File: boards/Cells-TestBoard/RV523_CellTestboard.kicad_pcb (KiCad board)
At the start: 4 copper layers, 100 x 100 mm, 26 parts

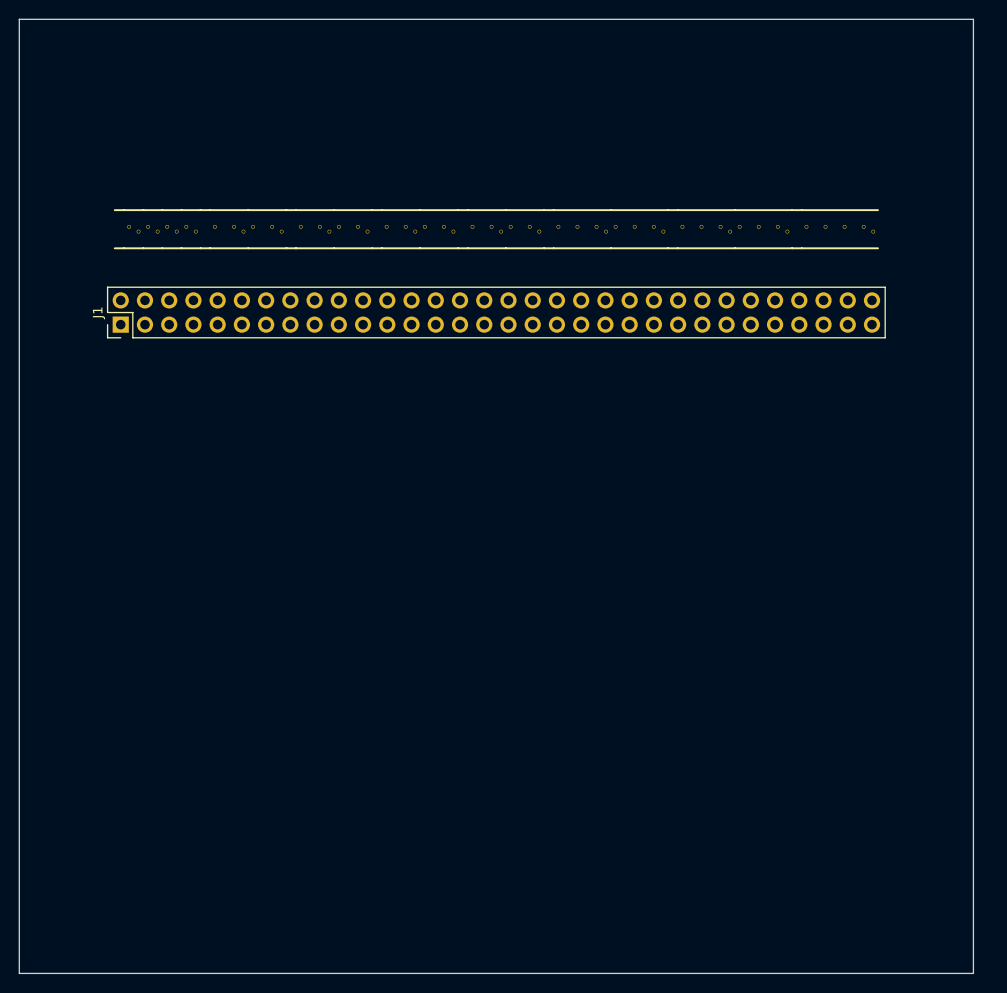
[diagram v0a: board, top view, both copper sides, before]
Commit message: Cell test board: all components placed and routed, except supply rails.
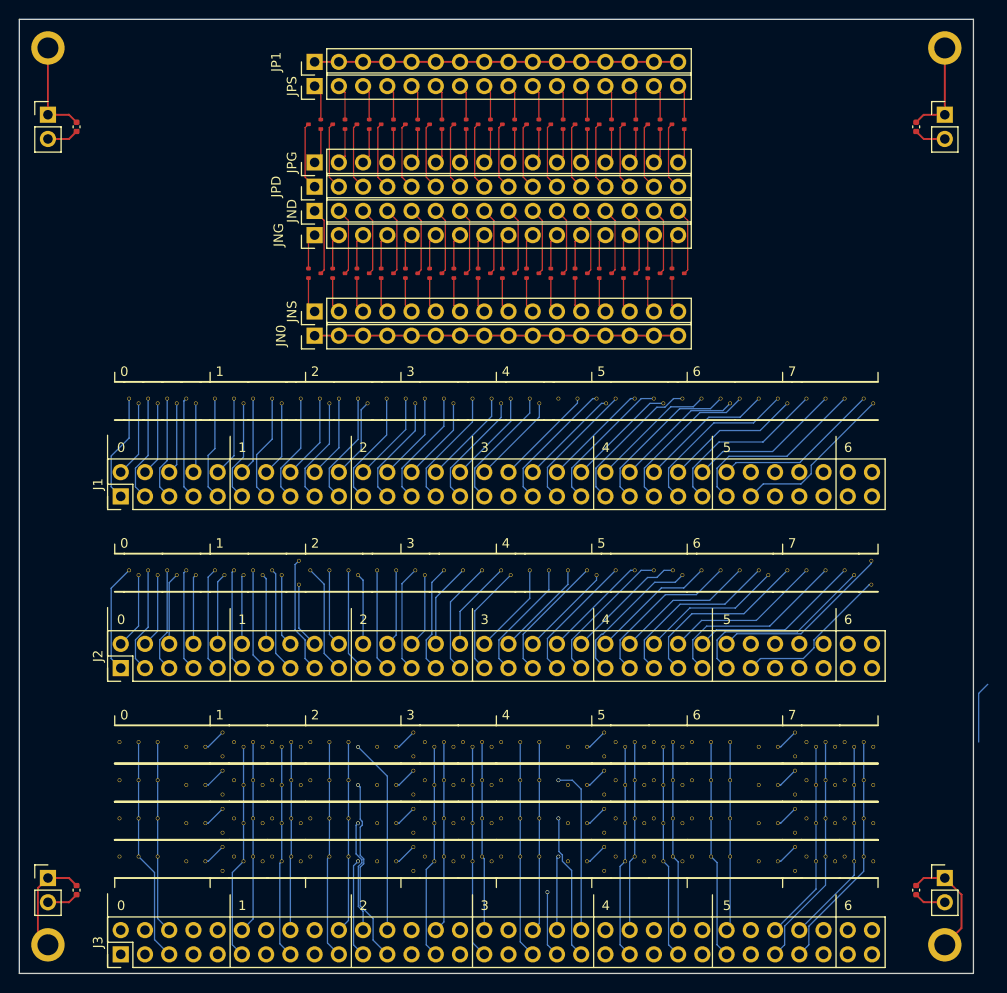
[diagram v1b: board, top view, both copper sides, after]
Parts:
- added AOI211_1: , RV523:AOI211, F.Cu at (62.0, 56.0)
- added AOI21_1: , RV523:AOI21, F.Cu at (30.0, 56.0)
- added AOI22_1: , RV523:AOI22, F.Cu at (44.0, 56.0)
- added DECAP1: , Capacitor_SMD:C_0402_1005Metric, F.Cu at (6.00, 11.3)
- added DECAP2: , Capacitor_SMD:C_0402_1005Metric, F.Cu at (94.0, 11.3)
- added DECAP3: , Capacitor_SMD:C_0402_1005Metric, F.Cu at (6.00, 91.3)
- added DECAP4: , Capacitor_SMD:C_0402_1005Metric, F.Cu at (94.0, 91.3)
- added DECAP_10: , RV523:DECAP, F.Cu at (10.0, 56.0)
- added DECAP_11: , RV523:DECAP, F.Cu at (19.0, 56.0)
- added DECAP_13: , RV523:DECAP, F.Cu at (36.0, 56.0)
- added DECAP_14: , RV523:DECAP, F.Cu at (43.0, 56.0)
- added DECAP_15: , RV523:DECAP, F.Cu at (52.0, 56.0)
- added DECAP_16: , RV523:DECAP, F.Cu at (61.0, 56.0)
- added DECAP_17: , RV523:DECAP, F.Cu at (70.0, 56.0)
- added DECAP_18: , RV523:DECAP, F.Cu at (79.0, 56.0)
- added DECAP_LED_12: , RV523:DECAP_LED, F.Cu at (28.0, 56.0)
- added DECAP_LED_19: , RV523:DECAP_LED, F.Cu at (88.0, 56.0)
- added J2: , Connector_PinHeader_2.54mm:PinHeader_2x32_P2.54mm_Vertical, F.Cu at (10.6, 68.0)
- added J3: , Connector_PinHeader_2.54mm:PinHeader_2x32_P2.54mm_Vertical, F.Cu at (10.6, 98.0)
- added JN0: , Connector_PinHeader_2.54mm:PinHeader_1x16_P2.54mm_Vertical, F.Cu at (30.9, 33.2)
- added JND: , Connector_PinHeader_2.54mm:PinHeader_1x16_P2.54mm_Vertical, F.Cu at (30.9, 20.1)
- added JNG: , Connector_PinHeader_2.54mm:PinHeader_1x16_P2.54mm_Vertical, F.Cu at (30.9, 22.6)
- added JNS: , Connector_PinHeader_2.54mm:PinHeader_1x16_P2.54mm_Vertical, F.Cu at (30.9, 30.6)
- added JP1: , Connector_PinHeader_2.54mm:PinHeader_1x16_P2.54mm_Vertical, F.Cu at (30.9, 4.46)
- added JPD: , Connector_PinHeader_2.54mm:PinHeader_1x16_P2.54mm_Vertical, F.Cu at (30.9, 17.5)
- added JPG: , Connector_PinHeader_2.54mm:PinHeader_1x16_P2.54mm_Vertical, F.Cu at (30.9, 15.0)
- added JPS: , Connector_PinHeader_2.54mm:PinHeader_1x16_P2.54mm_Vertical, F.Cu at (30.9, 7.00)
- added JSupply1: , Connector_PinHeader_2.54mm:PinHeader_1x02_P2.54mm_Vertical, F.Cu at (3.00, 10.0)
- added JSupply2: , Connector_PinHeader_2.54mm:PinHeader_1x02_P2.54mm_Vertical, F.Cu at (97.0, 10.0)
- added JSupply3: , Connector_PinHeader_2.54mm:PinHeader_1x02_P2.54mm_Vertical, F.Cu at (3.00, 90.0)
- added JSupply4: , Connector_PinHeader_2.54mm:PinHeader_1x02_P2.54mm_Vertical, F.Cu at (97.0, 90.0)
- added NOR4_1: , RV523:NOR4, F.Cu at (80.0, 56.0)
- added OAI211_1: , RV523:OAI211, F.Cu at (71.0, 56.0)
- added OAI21_1: , RV523:OAI21, F.Cu at (37.0, 56.0)
- added OAI22_1: , RV523:OAI22, F.Cu at (53.0, 56.0)
- added REF**: MountingHole_2.2mm_M2_ISO7380_Pad, MountingHole:MountingHole_2.2mm_M2_ISO7380_Pad, F.Cu at (97.0, 97.0)
- added REF**: MountingHole_2.2mm_M2_ISO7380_Pad, MountingHole:MountingHole_2.2mm_M2_ISO7380_Pad, F.Cu at (3.00, 3.00)
- added REF**: MountingHole_2.2mm_M2_ISO7380_Pad, MountingHole:MountingHole_2.2mm_M2_ISO7380_Pad, F.Cu at (3.00, 97.0)
- added REF**: MountingHole_2.2mm_M2_ISO7380_Pad, MountingHole:MountingHole_2.2mm_M2_ISO7380_Pad, F.Cu at (97.0, 3.00)
- added TINV_1: , RV523:TINV, F.Cu at (11.0, 56.0)
- added TINV_2: , RV523:TINV, F.Cu at (15.0, 56.0)
- added TINV_3: , RV523:TINV, F.Cu at (20.0, 56.0)
- added TINV_4: , RV523:TINV, F.Cu at (24.0, 56.0)
- added genblk1[10].N: NMOS, RV523:SOT523, F.Cu at (53.8, 26.6)
- added genblk1[10].P: PMOS, RV523:SOT523, F.Cu at (53.8, 11.0)
- added genblk1[11].N: NMOS, RV523:SOT523, F.Cu at (56.4, 26.6)
- added genblk1[11].P: PMOS, RV523:SOT523, F.Cu at (56.4, 11.0)
- added genblk1[12].N: NMOS, RV523:SOT523, F.Cu at (58.9, 26.6)
- added genblk1[12].P: PMOS, RV523:SOT523, F.Cu at (58.9, 11.0)
- added genblk1[13].N: NMOS, RV523:SOT523, F.Cu at (61.4, 26.6)
- added genblk1[13].P: PMOS, RV523:SOT523, F.Cu at (61.4, 11.0)
- added genblk1[14].N: NMOS, RV523:SOT523, F.Cu at (64.0, 26.6)
- added genblk1[14].P: PMOS, RV523:SOT523, F.Cu at (64.0, 11.0)
- added genblk1[15].N: NMOS, RV523:SOT523, F.Cu at (66.5, 26.6)
- added genblk1[15].P: PMOS, RV523:SOT523, F.Cu at (66.5, 11.0)
- added genblk1[16].N: NMOS, RV523:SOT523, F.Cu at (69.0, 26.6)
- added genblk1[16].P: PMOS, RV523:SOT523, F.Cu at (69.0, 11.0)
- added genblk1[1].N: NMOS, RV523:SOT523, F.Cu at (30.9, 26.6)
- added genblk1[1].P: PMOS, RV523:SOT523, F.Cu at (30.9, 11.0)
- added genblk1[2].N: NMOS, RV523:SOT523, F.Cu at (33.5, 26.6)
- added genblk1[2].P: PMOS, RV523:SOT523, F.Cu at (33.5, 11.0)
- added genblk1[3].N: NMOS, RV523:SOT523, F.Cu at (36.0, 26.6)
- added genblk1[3].P: PMOS, RV523:SOT523, F.Cu at (36.0, 11.0)
- added genblk1[4].N: NMOS, RV523:SOT523, F.Cu at (38.6, 26.6)
- added genblk1[4].P: PMOS, RV523:SOT523, F.Cu at (38.6, 11.0)
- added genblk1[5].N: NMOS, RV523:SOT523, F.Cu at (41.1, 26.6)
- added genblk1[5].P: PMOS, RV523:SOT523, F.Cu at (41.1, 11.0)
- added genblk1[6].N: NMOS, RV523:SOT523, F.Cu at (43.6, 26.6)
- added genblk1[6].P: PMOS, RV523:SOT523, F.Cu at (43.6, 11.0)
- added genblk1[7].N: NMOS, RV523:SOT523, F.Cu at (46.2, 26.6)
- added genblk1[7].P: PMOS, RV523:SOT523, F.Cu at (46.2, 11.0)
- added genblk1[8].N: NMOS, RV523:SOT523, F.Cu at (48.7, 26.6)
- added genblk1[8].P: PMOS, RV523:SOT523, F.Cu at (48.7, 11.0)
- added genblk1[9].N: NMOS, RV523:SOT523, F.Cu at (51.3, 26.6)
- added genblk1[9].P: PMOS, RV523:SOT523, F.Cu at (51.3, 11.0)
- added genblk2[0].genblk1[0].D: , RV523:DECAP_LED, F.Cu at (20.0, 74.0)
- added genblk2[0].genblk1[0].L: , RV523:D_LATCH, F.Cu at (10.0, 74.0)
- added genblk2[0].genblk1[0].R1: , RV523:TINV, F.Cu at (22.0, 74.0)
- added genblk2[0].genblk1[0].R2: , RV523:TINV, F.Cu at (26.0, 74.0)
- added genblk2[0].genblk1[1].D: , RV523:DECAP_LED, F.Cu at (20.0, 78.0)
- added genblk2[0].genblk1[1].L: , RV523:D_LATCH, F.Cu at (10.0, 78.0)
- added genblk2[0].genblk1[1].R1: , RV523:TINV, F.Cu at (22.0, 78.0)
- added genblk2[0].genblk1[1].R2: , RV523:TINV, F.Cu at (26.0, 78.0)
- added genblk2[0].genblk1[2].D: , RV523:DECAP_LED, F.Cu at (20.0, 82.0)
- added genblk2[0].genblk1[2].L: , RV523:D_LATCH, F.Cu at (10.0, 82.0)
- added genblk2[0].genblk1[2].R1: , RV523:TINV, F.Cu at (22.0, 82.0)
- added genblk2[0].genblk1[2].R2: , RV523:TINV, F.Cu at (26.0, 82.0)
- added genblk2[0].genblk1[3].D: , RV523:DECAP_LED, F.Cu at (20.0, 86.0)
- added genblk2[0].genblk1[3].L: , RV523:D_LATCH, F.Cu at (10.0, 86.0)
- added genblk2[0].genblk1[3].R1: , RV523:TINV, F.Cu at (22.0, 86.0)
- added genblk2[0].genblk1[3].R2: , RV523:TINV, F.Cu at (26.0, 86.0)
- added genblk2[1].genblk1[0].D: , RV523:DECAP_LED, F.Cu at (40.0, 74.0)
- added genblk2[1].genblk1[0].L: , RV523:D_LATCH, F.Cu at (30.0, 74.0)
- added genblk2[1].genblk1[0].R1: , RV523:TINV, F.Cu at (42.0, 74.0)
- added genblk2[1].genblk1[0].R2: , RV523:TINV, F.Cu at (46.0, 74.0)
- added genblk2[1].genblk1[1].D: , RV523:DECAP_LED, F.Cu at (40.0, 78.0)
- added genblk2[1].genblk1[1].L: , RV523:D_LATCH, F.Cu at (30.0, 78.0)
- added genblk2[1].genblk1[1].R1: , RV523:TINV, F.Cu at (42.0, 78.0)
- added genblk2[1].genblk1[1].R2: , RV523:TINV, F.Cu at (46.0, 78.0)
- added genblk2[1].genblk1[2].D: , RV523:DECAP_LED, F.Cu at (40.0, 82.0)
- added genblk2[1].genblk1[2].L: , RV523:D_LATCH, F.Cu at (30.0, 82.0)
- added genblk2[1].genblk1[2].R1: , RV523:TINV, F.Cu at (42.0, 82.0)
- added genblk2[1].genblk1[2].R2: , RV523:TINV, F.Cu at (46.0, 82.0)
- added genblk2[1].genblk1[3].D: , RV523:DECAP_LED, F.Cu at (40.0, 86.0)
- added genblk2[1].genblk1[3].L: , RV523:D_LATCH, F.Cu at (30.0, 86.0)
- added genblk2[1].genblk1[3].R1: , RV523:TINV, F.Cu at (42.0, 86.0)
- added genblk2[1].genblk1[3].R2: , RV523:TINV, F.Cu at (46.0, 86.0)
- added genblk2[2].genblk1[0].D: , RV523:DECAP_LED, F.Cu at (60.0, 74.0)
- added genblk2[2].genblk1[0].L: , RV523:D_LATCH, F.Cu at (50.0, 74.0)
- added genblk2[2].genblk1[0].R1: , RV523:TINV, F.Cu at (62.0, 74.0)
- added genblk2[2].genblk1[0].R2: , RV523:TINV, F.Cu at (66.0, 74.0)
- added genblk2[2].genblk1[1].D: , RV523:DECAP_LED, F.Cu at (60.0, 78.0)
- added genblk2[2].genblk1[1].L: , RV523:D_LATCH, F.Cu at (50.0, 78.0)
- added genblk2[2].genblk1[1].R1: , RV523:TINV, F.Cu at (62.0, 78.0)
- added genblk2[2].genblk1[1].R2: , RV523:TINV, F.Cu at (66.0, 78.0)
- added genblk2[2].genblk1[2].D: , RV523:DECAP_LED, F.Cu at (60.0, 82.0)
- added genblk2[2].genblk1[2].L: , RV523:D_LATCH, F.Cu at (50.0, 82.0)
- added genblk2[2].genblk1[2].R1: , RV523:TINV, F.Cu at (62.0, 82.0)
- added genblk2[2].genblk1[2].R2: , RV523:TINV, F.Cu at (66.0, 82.0)
- added genblk2[2].genblk1[3].D: , RV523:DECAP_LED, F.Cu at (60.0, 86.0)
- added genblk2[2].genblk1[3].L: , RV523:D_LATCH, F.Cu at (50.0, 86.0)
- added genblk2[2].genblk1[3].R1: , RV523:TINV, F.Cu at (62.0, 86.0)
- added genblk2[2].genblk1[3].R2: , RV523:TINV, F.Cu at (66.0, 86.0)
- added genblk2[3].genblk1[0].D: , RV523:DECAP_LED, F.Cu at (80.0, 74.0)
- added genblk2[3].genblk1[0].L: , RV523:D_LATCH, F.Cu at (70.0, 74.0)
- added genblk2[3].genblk1[0].R1: , RV523:TINV, F.Cu at (82.0, 74.0)
- added genblk2[3].genblk1[0].R2: , RV523:TINV, F.Cu at (86.0, 74.0)
- added genblk2[3].genblk1[1].D: , RV523:DECAP_LED, F.Cu at (80.0, 78.0)
- added genblk2[3].genblk1[1].L: , RV523:D_LATCH, F.Cu at (70.0, 78.0)
- added genblk2[3].genblk1[1].R1: , RV523:TINV, F.Cu at (82.0, 78.0)
- added genblk2[3].genblk1[1].R2: , RV523:TINV, F.Cu at (86.0, 78.0)
- added genblk2[3].genblk1[2].D: , RV523:DECAP_LED, F.Cu at (80.0, 82.0)
- added genblk2[3].genblk1[2].L: , RV523:D_LATCH, F.Cu at (70.0, 82.0)
- added genblk2[3].genblk1[2].R1: , RV523:TINV, F.Cu at (82.0, 82.0)
- added genblk2[3].genblk1[2].R2: , RV523:TINV, F.Cu at (86.0, 82.0)
- added genblk2[3].genblk1[3].D: , RV523:DECAP_LED, F.Cu at (80.0, 86.0)
- added genblk2[3].genblk1[3].L: , RV523:D_LATCH, F.Cu at (70.0, 86.0)
- added genblk2[3].genblk1[3].R1: , RV523:TINV, F.Cu at (82.0, 86.0)
- added genblk2[3].genblk1[3].R2: , RV523:TINV, F.Cu at (86.0, 86.0)
- moved DECAP_1 18.0 mm to (10.0, 38.0)
- moved DECAP_2 18.0 mm to (19.0, 38.0)
- moved DECAP_3 18.0 mm to (28.0, 38.0)
- moved DECAP_4 18.0 mm to (37.0, 38.0)
- moved DECAP_5 18.0 mm to (46.0, 38.0)
- moved DECAP_6 18.0 mm to (55.0, 38.0)
- moved DECAP_7 18.0 mm to (68.0, 38.0)
- moved DECAP_8 18.0 mm to (81.0, 38.0)
- moved J1 18.0 mm to (10.6, 50.0)
- moved NAND2_1 18.0 mm to (20.0, 38.0)
- moved NAND2_2 18.0 mm to (24.0, 38.0)
- moved NAND2_3 18.0 mm to (29.0, 38.0)
- moved NAND2_4 18.0 mm to (33.0, 38.0)
- moved NAND3_1 18.0 mm to (56.0, 38.0)
- moved NAND3_2 18.0 mm to (62.0, 38.0)
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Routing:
- net J3pins.1: track 0.00 -> 87.8 mm
- net J3pins[24]: track 0.00 -> 84.0 mm, vias 0 -> 1
- net J3pins[23]: track 0.00 -> 83.9 mm, vias 0 -> 1
- net J3pins[40]: track 0.00 -> 83.3 mm, vias 0 -> 1
- net J3pins[64]: track 0.00 -> 82.6 mm
- net GND: track 0.00 -> 81.7 mm
- net J3pins.2: track 0.00 -> 81.2 mm
- net J3pins[39]: track 0.00 -> 81.0 mm, vias 0 -> 1
- net J3pins.3: track 0.00 -> 80.4 mm
- net J3pins[63]: track 0.00 -> 80.1 mm
- net J3pins[22]: track 0.00 -> 76.3 mm, vias 0 -> 1
- net J3pins[21]: track 0.00 -> 74.6 mm, vias 0 -> 1
- net J3pins.4: track 0.00 -> 73.6 mm
- net J3pins[38]: track 0.00 -> 73.5 mm, vias 0 -> 1
- net J3pins[37]: track 0.00 -> 72.5 mm, vias 0 -> 1
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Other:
- board text added: "0"
- board text added: "1"
- board text added: "2"
- board text added: "3"
- board text added: "4"
- board text added: "5"
- board text added: "6"
- board text added: "7"

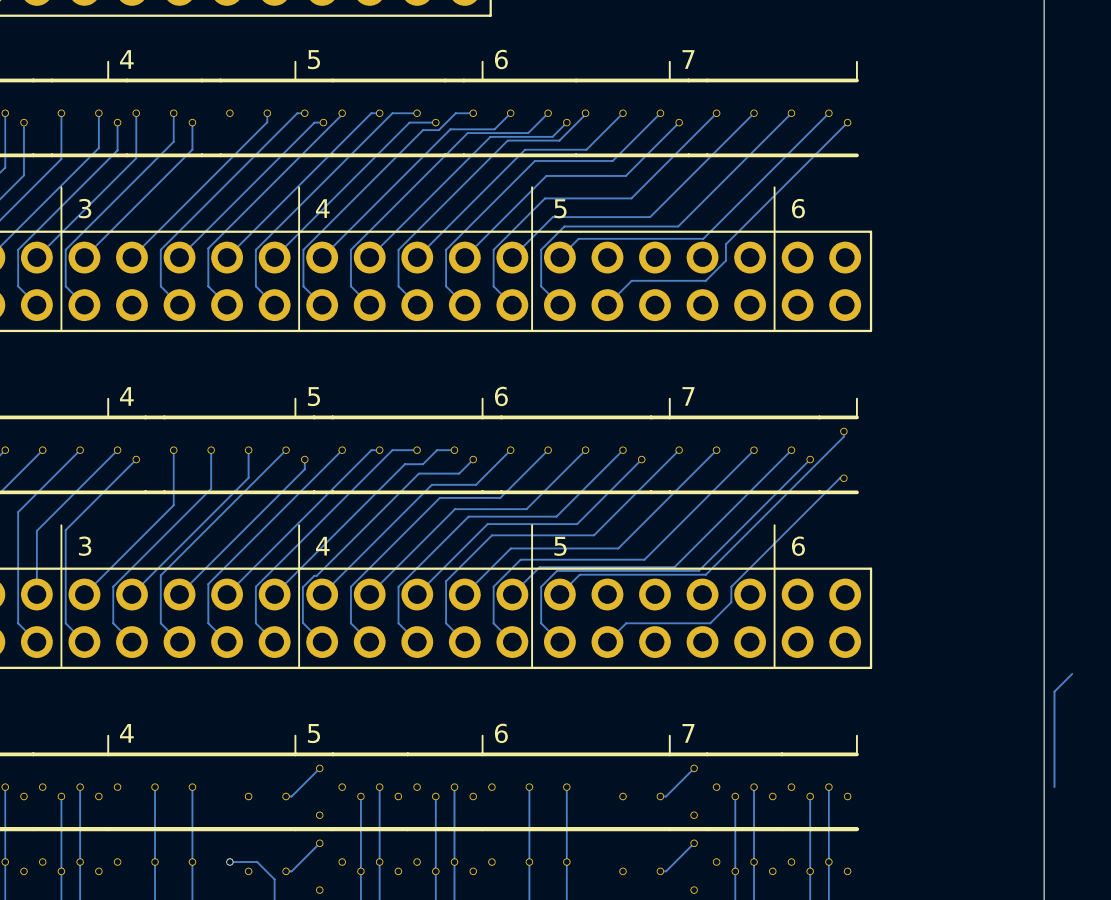
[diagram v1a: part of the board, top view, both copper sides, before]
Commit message: One track missing. Also remove one loose track.
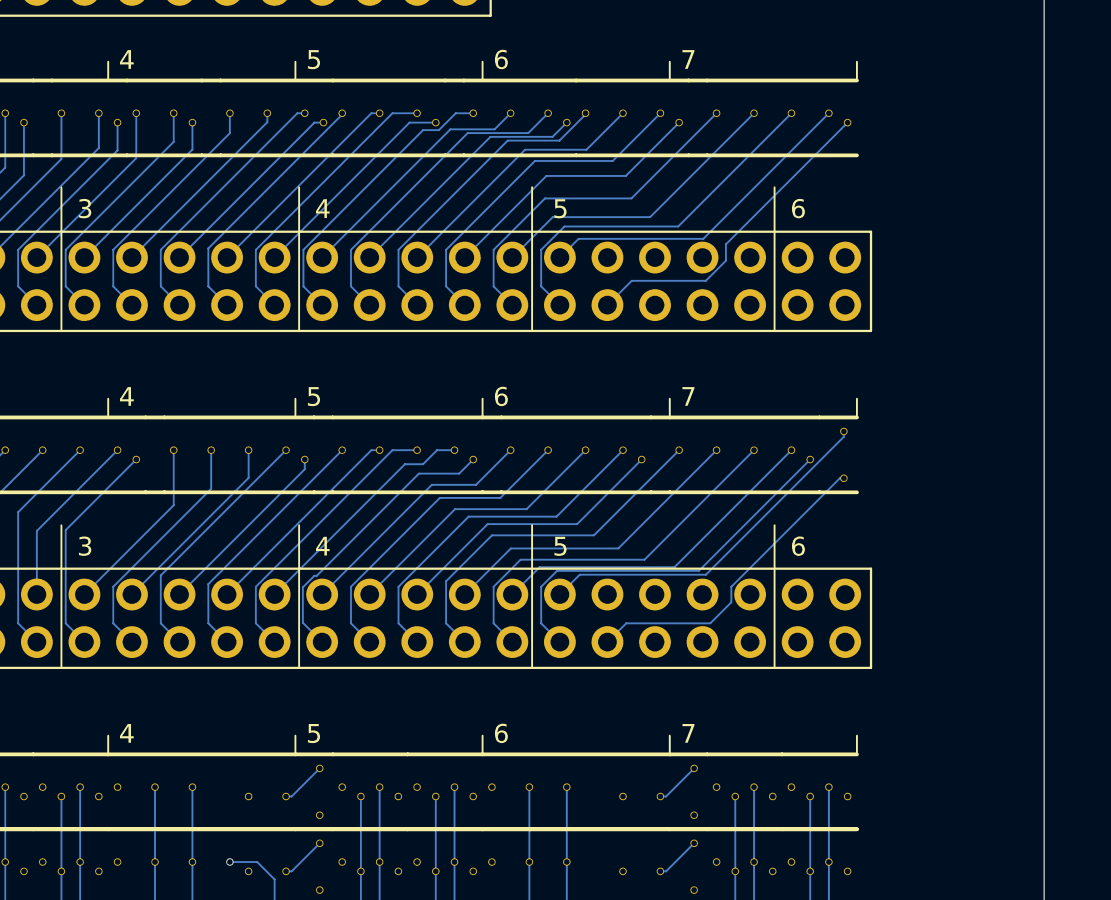
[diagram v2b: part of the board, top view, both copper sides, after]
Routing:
- net J1pins.33: track 0.00 -> 13.2 mm
- net (no net): track 6.44 -> 0.00 mm
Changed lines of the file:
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@@
-	)
-	(segment
-		(start 100.551 70.649)
-		(end 100.551 75.75)
-		(width 0.1)
-		(layer "B.Cu")
-		(net 0)
-	)
-	(segment
-		(start 101.5 69.7)
-		(end 100.551 70.649)
-		(width 0.1)
-		(layer "B.Cu")
-		(net 0)
 	)
 	(segment
@@
 	)
 	(segment
+		(start 56.5 40.814372)
+		(end 50.269 47.045372)
+		(width 0.1)
+		(layer "B.Cu")
+		(net 22)
+	)
+	(segment
+		(start 56.5 39.75)
+		(end 56.5 40.814372)
+		(width 0.1)
+		(layer "B.Cu")
+		(net 22)
+	)
+	(segment
+		(start 50.269 47.045372)
+		(end 50.269 48.999)
+		(width 0.1)
+		(layer "B.Cu")
+		(net 22)
+	)
+	(segment
+		(start 50.269 48.999)
+		(end 51.27 50)
+		(width 0.1)
+		(layer "B.Cu")
+		(net 22)
+	)
+	(segment

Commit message: Final PCB
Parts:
- moved JSupply3 3.23 mm to (5.00, 92.5), turned to 180 degrees
- moved JSupply4 3.23 mm to (95.0, 92.5), turned to 180 degrees
- moved DECAP1 2.00 mm to (8.00, 11.3)
- moved DECAP2 2.00 mm to (92.0, 11.3)
- moved DECAP3 2.00 mm to (8.00, 91.3), turned to -90 degrees
- moved DECAP4 2.00 mm to (92.0, 91.3), turned to -90 degrees
- moved JSupply1 2.00 mm to (5.00, 10.0)
- moved JSupply2 2.00 mm to (95.0, 10.0)
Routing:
- net GND: track 81.7 -> 376.0 mm
- net VDD: track 51.4 -> 205.9 mm
- added copper zone on B.Cu, net (none)
- added copper zone on F.Cu, net (none)
- added copper zone on In1.Cu, net (none)
- added copper zone on In2.Cu, net VDD
